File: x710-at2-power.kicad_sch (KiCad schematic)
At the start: 121 parts, among them U4 EZX710AT2_S_LMR5

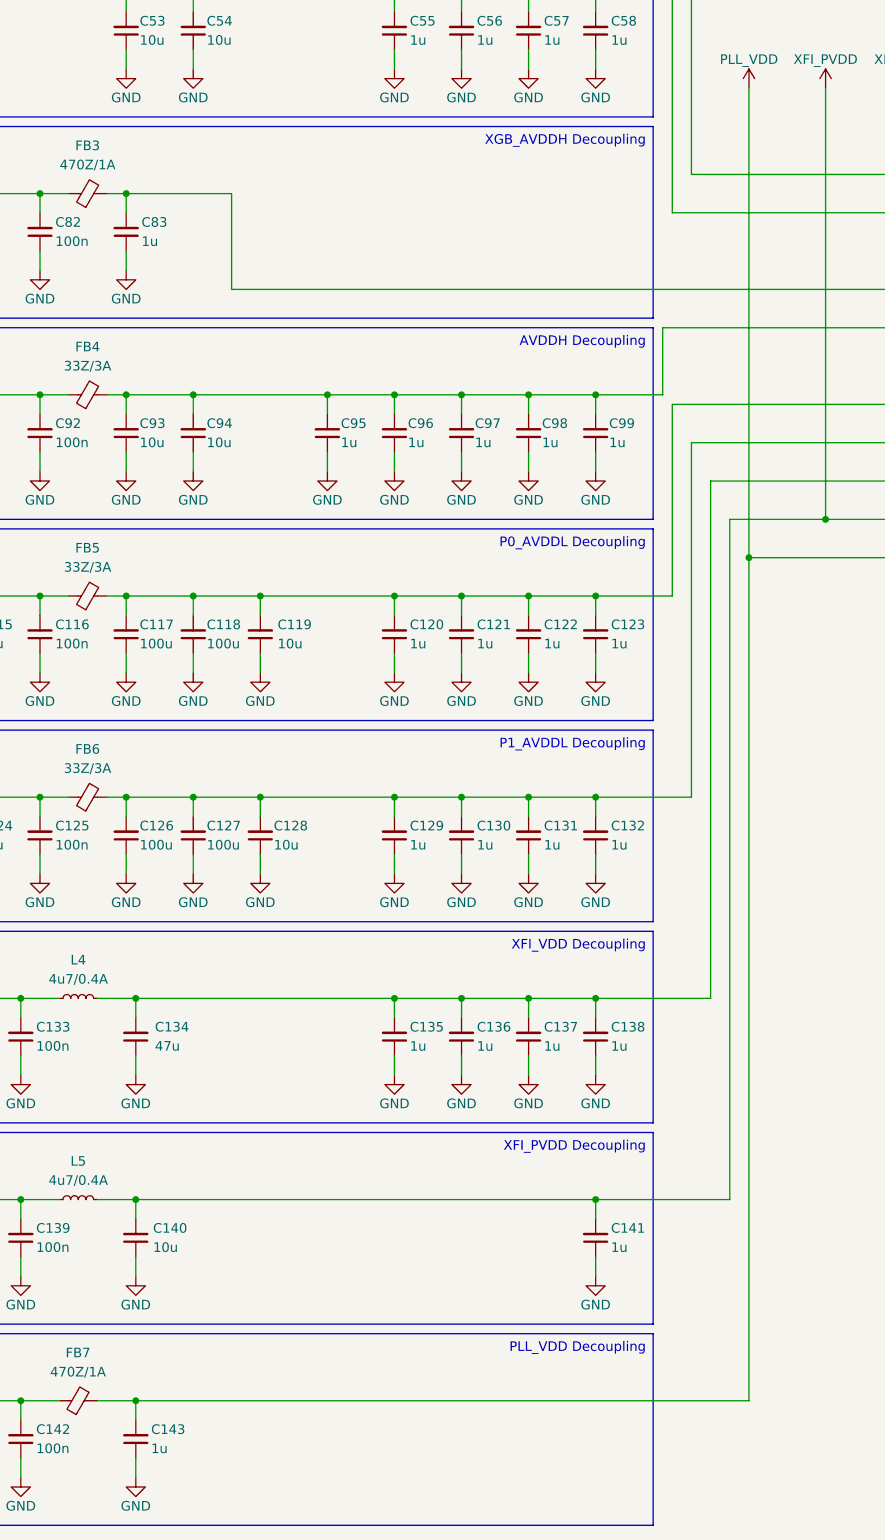
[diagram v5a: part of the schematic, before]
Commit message: [#85196] Clear ERC, minor schematic fixes
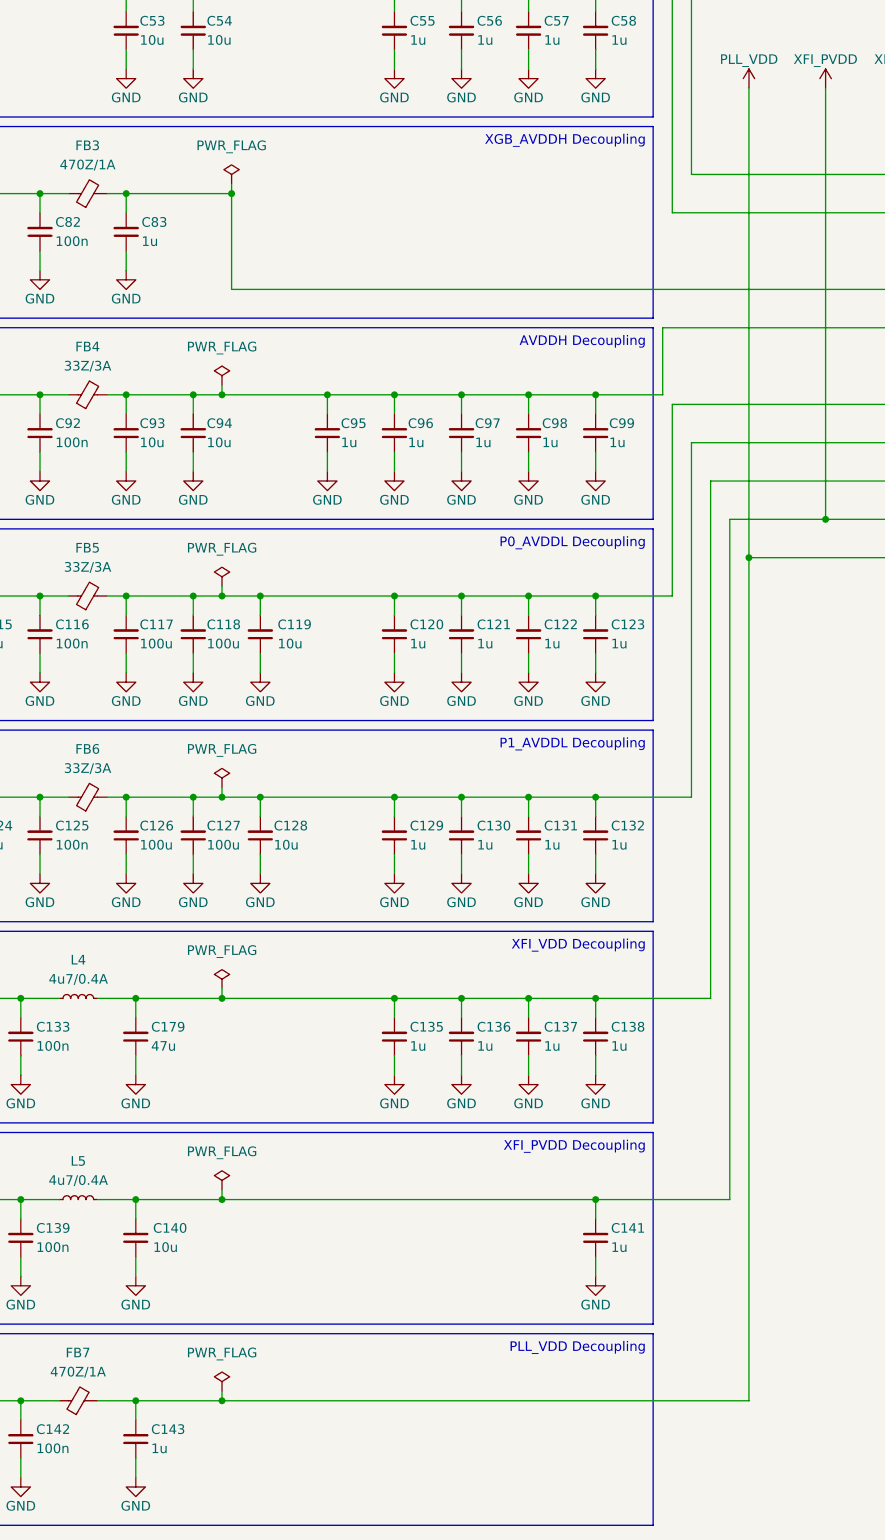
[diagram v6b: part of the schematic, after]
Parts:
- removed C134: C_47u_50V_X7R_0402, antmicro-footprints:C_0402_1005Metric, symbol antmicroCapacitors0402:C_47u_50V_X7R_0402
- added C179: C_47u_0603, antmicro-footprints:C_0603_1608Metric, symbol antmicroCapacitors0603:C_47u_0603
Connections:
- net GND: now also C179.1
- net XFI_VDD: now also C179.2

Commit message: [#85196] Re-annotate schematic
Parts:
- renumbered C54 to C100, C55 to C101, C56 to C102, C57 to C103, C58 to C104, C59 to C105, C60 to C106, C61 to C107, C62 to C108, C63 to C109, C64 to C110, C65 to C111, C66 to C112, C67 to C113, C68 to C114, C69 to C115, C70 to C116, C71 to C117, C72 to C118, C73 to C119, C74 to C120, C75 to C121, C76 to C122, C77 to C123, C78 to C124, C79 to C125, C80 to C126, C81 to C127, C82 to C128, C83 to C129, C84 to C130, C85 to C131, C86 to C132, C87 to C133, C88 to C134, C89 to C135, C90 to C136, C91 to C137, C92 to C138, C93 to C139, C94 to C140, C95 to C141, C96 to C142, C97 to C143, C98 to C144, C99 to C145, C100 to C146, C101 to C147, C102 to C148, C103 to C149, C104 to C150, C105 to C151, C106 to C152, C107 to C153, C108 to C154, C109 to C155, C110 to C156, C111 to C157, C112 to C158, C113 to C159, C114 to C160, C115 to C161, C116 to C162, C117 to C163, C118 to C164, C119 to C165, C120 to C166, C121 to C167, C122 to C168, C123 to C169, C124 to C170, C125 to C171, C126 to C172, C127 to C173, C128 to C174, C129 to C175, C130 to C176, C131 to C177, C132 to C178, C133 to C179, C179 to C180, C135 to C181, C136 to C182, C137 to C183, C138 to C184, C139 to C185, C140 to C186, C141 to C187, C142 to C188, C143 to C189, C32 to C78, C33 to C79, C34 to C80, C35 to C81, C36 to C82, C37 to C83, C38 to C84, C39 to C85, C40 to C86, C41 to C87, C42 to C88, C43 to C89, C44 to C90, C45 to C91, C46 to C92, C47 to C93, C48 to C94, C49 to C95, C50 to C96, C51 to C97, C52 to C98, C53 to C99, L5 to L10, L3 to L8, L4 to L9, U4 to U9
